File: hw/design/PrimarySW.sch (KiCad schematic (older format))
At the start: 33 parts

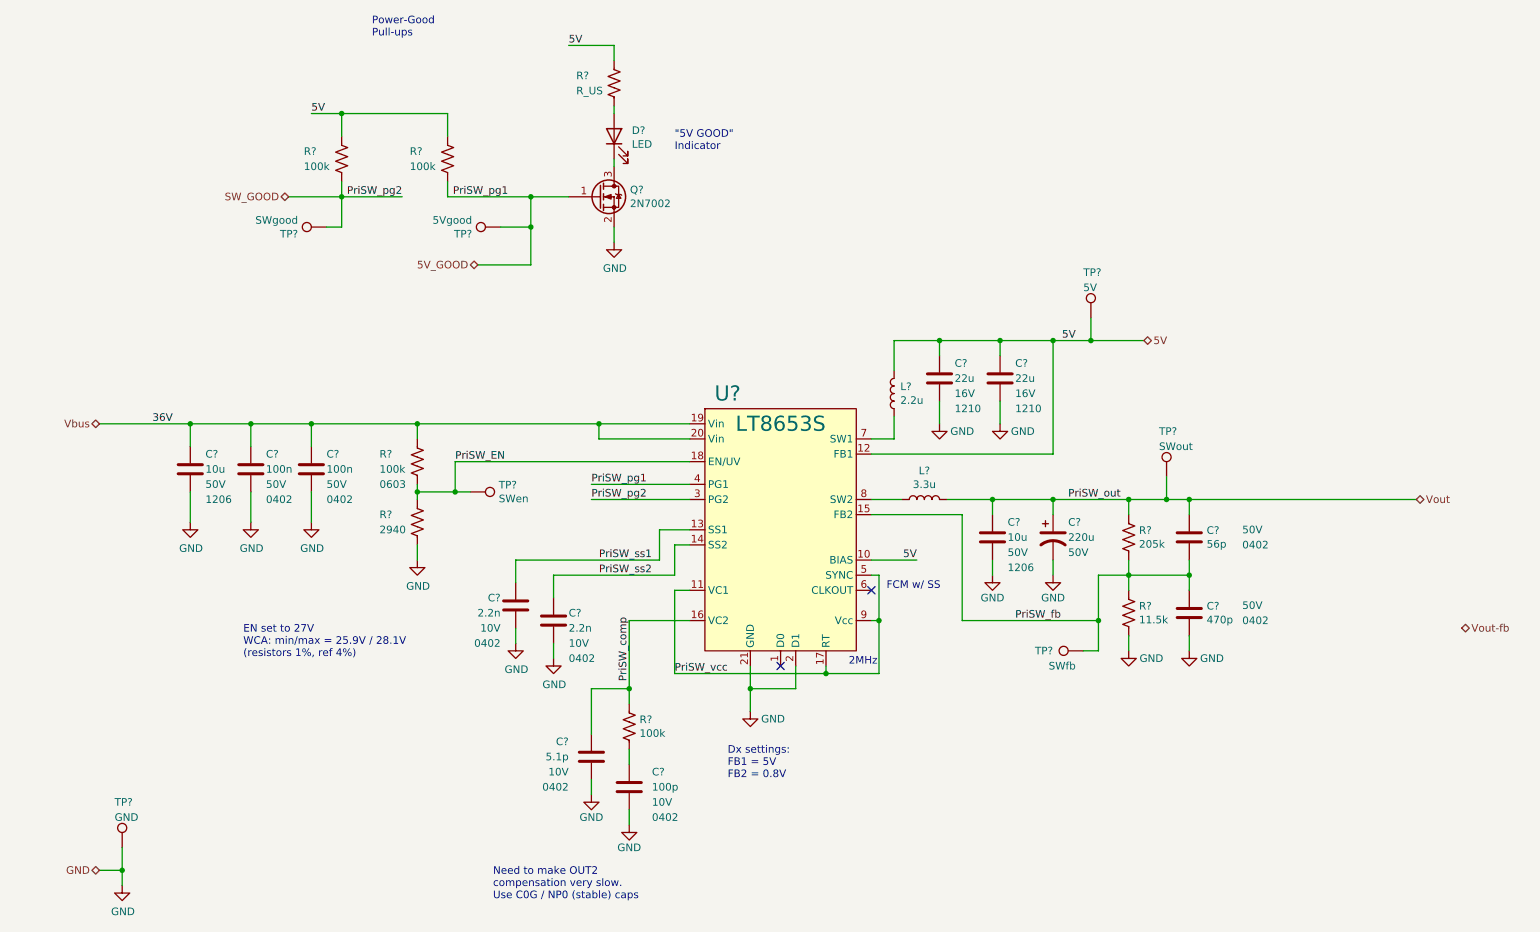
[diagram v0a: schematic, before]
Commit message: label/net reorg, primary SW starting
some reorganization of top-level naming for nets and hierarchical pins

fixed a few part selection issues

started on primary switcher sheet
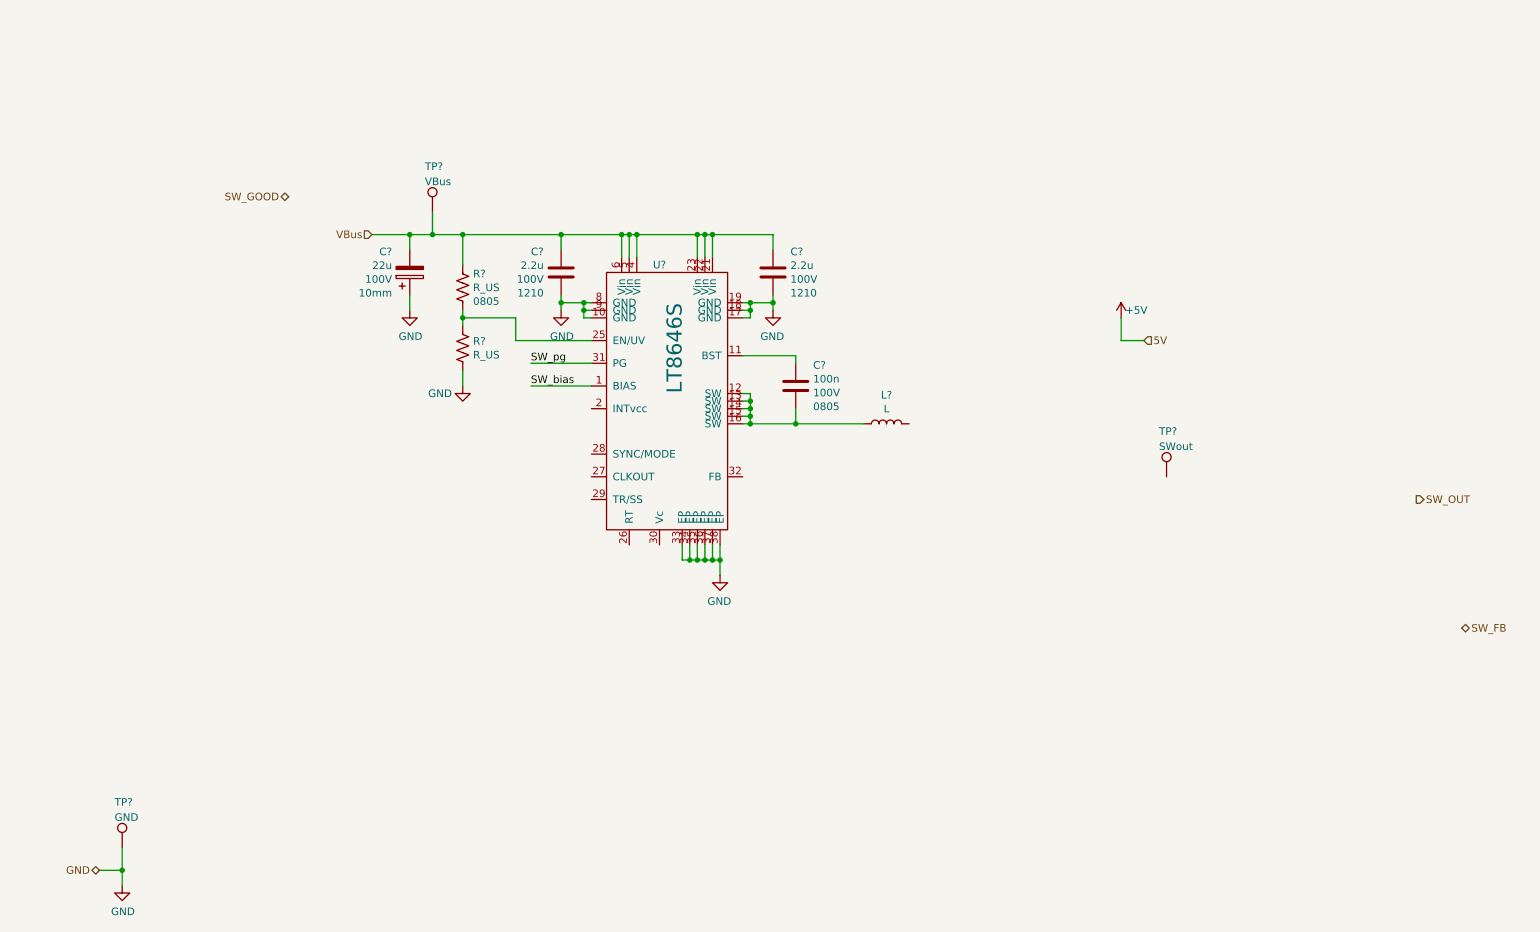
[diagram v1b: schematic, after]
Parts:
- removed C? (x2): 22u, Capacitor_SMD:C_1210_3225Metric_Pad1.42x2.65mm_HandSolder, symbol Device:C
- removed C?: 10u, Resistor_SMD:R_1206_3216Metric_Pad1.42x1.75mm_HandSolder, symbol Device:C
- removed C? (x2): 100n, Capacitor_SMD:C_0603_1608Metric, symbol Device:C
- removed C? (x2): 2.2n, Capacitor_SMD:C_0603_1608Metric, symbol Device:C
- removed C?: 100p, Capacitor_SMD:C_0603_1608Metric, symbol Device:C
- removed C?: 56p, Resistor_SMD:R_0603_1608Metric, symbol Device:C
- removed C?: 470p, Resistor_SMD:R_0603_1608Metric, symbol Device:C
- removed C?: 10u, Capacitor_SMD:C_1206_3216Metric_Pad1.42x1.75mm_HandSolder, symbol Device:C
- removed C?: 220u, symbol Device:CP1
- removed C?: 5.1p, Capacitor_SMD:C_0603_1608Metric, symbol Device:C
- removed D?: LED, LED_SMD:LED_0603_1608Metric, symbol Device:LED
- removed L?: 2.2u, Inductor_SMD:L_Coilcraft_XxL4020, symbol Device:L
- removed L?: 3.3u, Inductor_SMD:L_Coilcraft_XAL5030, symbol Device:L
- removed Q?: 2N7002, Package_TO_SOT_SMD:SOT-323_SC-70, symbol Device:Q_NMOS_GSD
- removed R?: 205k, Resistor_SMD:R_0603_1608Metric, symbol Device:R_US
- removed R?: 11.5k, Resistor_SMD:R_0603_1608Metric, symbol Device:R_US
- removed R? (x3): 100k, Resistor_SMD:R_0603_1608Metric, symbol Device:R_US
- removed R?: 2940, Resistor_SMD:R_0603_1608Metric, symbol Device:R_US
- removed R?: 100k, Resistor_SMD:R_0805_2012Metric, symbol Device:R_US
- removed R?: R_US, Resistor_SMD:R_0603_1608Metric, symbol Device:R_US
- removed TP?: 5V, TestPoint:TestPoint_Keystone_5000-5004_Miniature, symbol Connector:TestPoint
- removed TP?: SWfb, TestPoint:TestPoint_Keystone_5000-5004_Miniature, symbol Connector:TestPoint
- removed TP?: SWgood, TestPoint:TestPoint_Keystone_5000-5004_Miniature, symbol Connector:TestPoint
- removed TP?: 5Vgood, TestPoint:TestPoint_Keystone_5000-5004_Miniature, symbol Connector:TestPoint
- removed TP?: SWen, TestPoint:TestPoint_Keystone_5000-5004_Miniature, symbol Connector:TestPoint
- removed U?: LT8653S, symbol pps_klib:LT8653S
- added C?: 22u, symbol Device:CP
- added C? (x2): 2.2u, Capacitor_SMD:C_1210_3225Metric_Pad1.42x2.65mm_HandSolder, symbol Device:C
- added C?: 100n, symbol Device:C
- added L?: L, symbol Device:L
- added R?: R_US, Resistor_SMD:R_0805_2012Metric_Pad1.15x1.40mm_HandSolder, symbol Device:R_US
- added R?: R_US, Resistor_SMD:R_0603_1608Metric, symbol Device:R_US
- added TP?: VBus, TestPoint:TestPoint_Keystone_5000-5004_Miniature, symbol Connector:TestPoint
- added U?: LT8646S, symbol pps_klib:LT8646S
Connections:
- net GND: now also C?.1, C?.1, C?.1, R?.2, U?.10 (GND), U?.17 (GND), U?.18 (GND), U?.19 (GND), U?.33 (EP), U?.34 (EP), U?.35 (EP), U?.36 (EP), U?.37 (EP), U?.38 (EP), U?.8 (GND), U?.9 (GND)
- net Vout: no longer names the net of TP?.1
- new net: C?.1, U?.11 (BST)
- new net: C?.2, L?.1, U?.12 (SW), U?.13 (SW), U?.14 (SW), U?.15 (SW), U?.16 (SW)
- new net: R?.1, R?.2, U?.25 (EN/UV)
- new net SW_bias: U?.1 (BIAS)
- new net SW_pg: U?.31 (PG)
- new net VBus: C?.2, C?.2, C?.2, R?.1, TP?.1, U?.21 (Vin), U?.22 (Vin), U?.23 (Vin), U?.4 (Vin), U?.5 (Vin), U?.6 (Vin)
- no-connect marks 2 -> 0
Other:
- note removed: ""5V GOOD"\nIndicator"
- note removed: "2MHz"
- note removed: "Dx settings:\nFB1 = 5V\nFB2 = 0.8V"
- note removed: "EN set to 27V\nWCA: min/max = 25.9V / 28.1V\n(resistors 1%, ref 4%)"
- note removed: "FCM w/ SS"
- note removed: "Need to make OUT2\ncompensation very slow.\nUse C0G / NP0 (stable) caps"
- note removed: "Power-Good\nPull-ups"

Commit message: sims, new devices, code started
made some simulations & calculations, started working on code (moved devices into individual header files), new devices chosen in library
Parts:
- removed C?: 22u, symbol Device:CP
- removed C? (x2): 2.2u, Capacitor_SMD:C_1210_3225Metric_Pad1.42x2.65mm_HandSolder, symbol Device:C
- removed C?: 100n, symbol Device:C
- removed L?: L, symbol Device:L
- removed R?: R_US, Resistor_SMD:R_0805_2012Metric_Pad1.15x1.40mm_HandSolder, symbol Device:R_US
- removed R?: R_US, Resistor_SMD:R_0603_1608Metric, symbol Device:R_US
- removed TP?: SWout, TestPoint:TestPoint_Keystone_5000-5004_Miniature, symbol Connector:TestPoint
- removed U?: LT8646S, symbol pps_klib:LT8646S
- added 49.9k, 49.9k?: R_US, Resistor_SMD:R_0603_1608Metric, symbol Device:R_US
- added C? (x3): 1u, Capacitor_SMD:C_0805_2012Metric_Pad1.15x1.40mm_HandSolder, symbol Device:C
- added C?: 1u, Capacitor_SMD:C_0603_1608Metric, symbol Device:C
- added C? (x2): 10n, Capacitor_SMD:C_0603_1608Metric, symbol Device:C
- added C?: 100n, Capacitor_SMD:C_0603_1608Metric, symbol Device:C
- added C? (x5): 10u, Capacitor_SMD:C_1206_3216Metric_Pad1.42x1.75mm_HandSolder, symbol Device:C
- added C?: 220u, symbol Device:CP
- added L?: L, symbol Device:L
- added Q?: 2N3906, Package_TO_SOT_THT:TO-92_Inline, symbol Transistor_BJT:2N3906
- added R? (x2): R_US, symbol Device:R_US
- added R?: 0, Resistor_SMD:R_0603_1608Metric, symbol Device:R_US
- added R?: 1k, symbol Device:R_US
- added U?: LT8637, symbol pps_klib:LT8637
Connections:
- net +5V: now also C?.2, U?.2 (BIAS)
- net GND: now also C?.1, C?.1, C?.1, C?.1, C?.1, C?.1, C?.1, C?.1, C?.1, C?.2, C?.2, R?.1, R?.1, R?.2, U?.13 (GND), U?.21 (EP), U?.4 (GND)
- net SW_FB: now also 49.9k?.1
- net SW_OUT: now also 49.9k.1, C?.1, C?.2, C?.2, C?.2, C?.2, C?.2, L?.2, R?.2
- net VBus: now also C?.1, C?.2, C?.2, U?.11 (VIN), U?.6 (VIN)
- new net: R?.2, U?.15 (SYNC/MODE)
- new net: R?.2, U?.17 (RT)
- new net: C?.2, U?.18 (TR/SS)
- new net: C?.1, Q?.3 (C), R?.1, U?.20 (FB)
- new net: Q?.1 (E), R?.1
- new net: 49.9k.2, 49.9k?.2, Q?.2 (B)
- new net Pre_BST: C?.2, U?.7 (BST)
- new net Pre_EN: U?.14 (EN)
- new net Pre_IVC: C?.2, U?.~ (INTVcc)
- new net Pre_PG: U?.1 (PG)
- new net Pre_SW: C?.1, L?.1, U?.10 (SW), U?.8 (SW), U?.9 (SW)
- no-connect marks 0 -> 1
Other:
- note added: "Ride-On-Top\nFeedback\nCircuit"
- note added: "TR/SS capacitance:\n1.2nF / msec startup"
- moved on the sheet: TP?

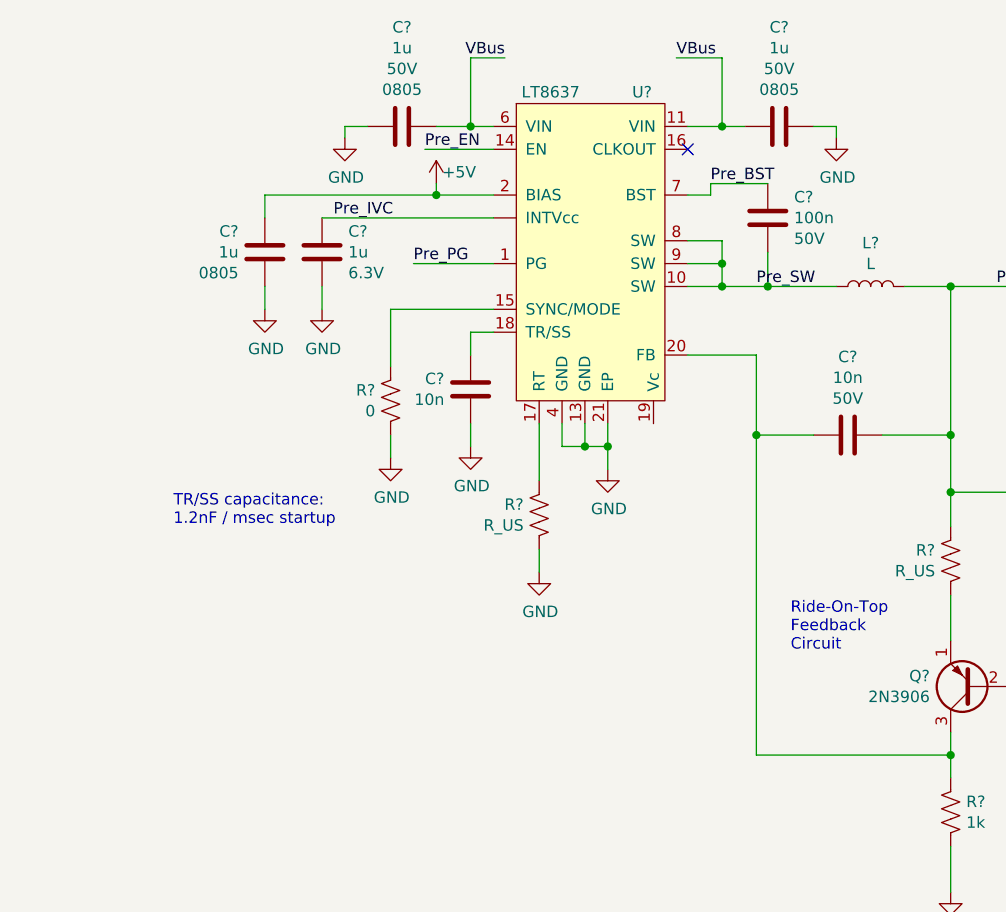
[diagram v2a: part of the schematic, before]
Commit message: rearchitect
new primary switcher : LT8637
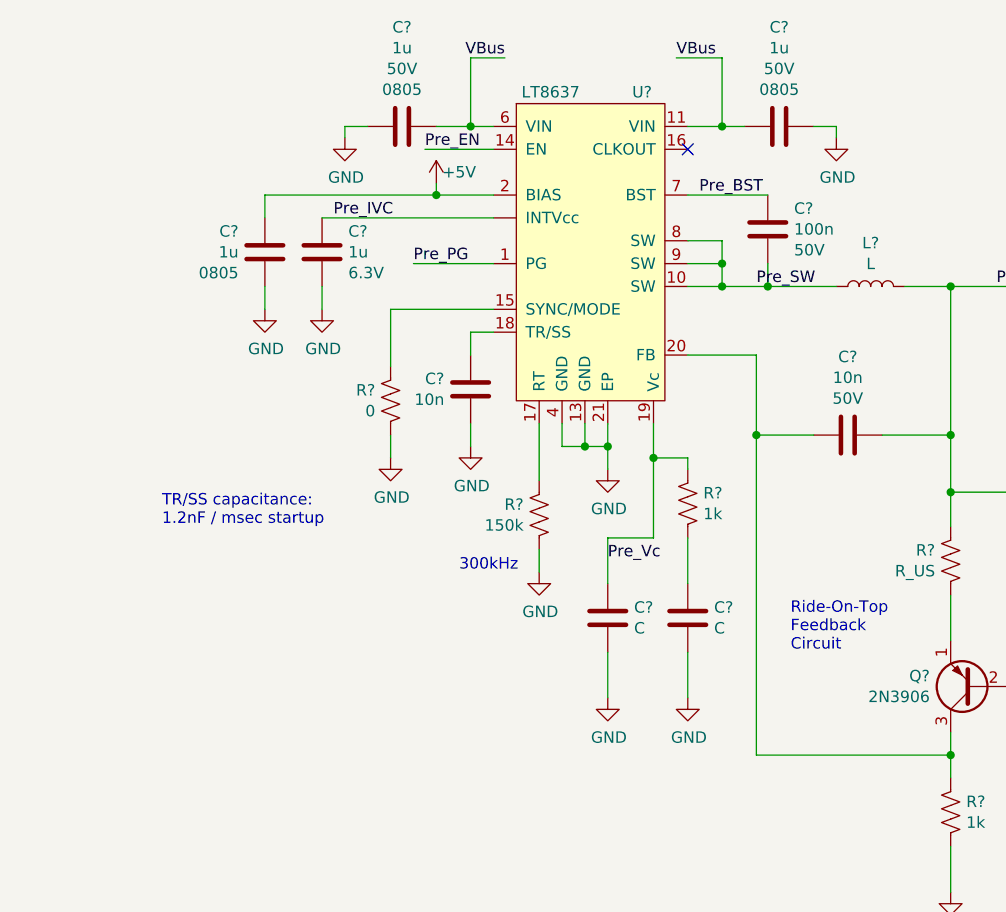
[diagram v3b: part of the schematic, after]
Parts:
- added C? (x2): C, Capacitor_SMD:C_0603_1608Metric, symbol Device:C
- added R?: 1k, Resistor_SMD:R_0603_1608Metric, symbol Device:R_US
- R?: value R_US -> 150k
- R?: footprint (none) -> Resistor_SMD:R_0603_1608Metric
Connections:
- net GND: now also C?.2, C?.2
- net Pre_Vc: now reaches U?.19 (Vc)
- net Pre_Vc: now also C?.1, R?.1
- new net: C?.1, R?.2
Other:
- note added: "300kHz"
- moved on the sheet: C?
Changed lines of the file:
@@
 	1    0    0    1
 $EndComp
-Text Notes 3750 4450 0    50   ~ 0
+Text Notes 3700 4450 0    50   ~ 0
 TR/SS capacitance:\n1.2nF / msec startup
 Wire Wire Line
@@
 L Device:C C?
 U 1 1 606F2507
-P 6350 3100
-F 0 "C?" H 6235 3009 50  0000 R CNN
-F 1 "100n" H 6235 3100 50  0000 R CNN
-F 2 "Capacitor_SMD:C_0603_1608Metric" H 6388 2950 50  0001 C CNN
-F 3 "~" H 6350 3100 50  0001 C CNN
-F 4 "TDK_CGA2B2X5R1C104K050BA" H 6350 3100 50  0001 C CNN "MfrNum"
-F 5 "50V" H 6235 3191 50  0000 R CNN "VRating"
-F 6 "0402" H 6235 3236 50  0001 R CNN "Size"
-	1    6350 3100
+P 6350 3150
+F 0 "C?" H 6235 3059 50  0000 R CNN
+F 1 "100n" H 6235 3150 50  0000 R CNN
+F 2 "Capacitor_SMD:C_0603_1608Metric" H 6388 3000 50  0001 C CNN
+F 3 "~" H 6350 3150 50  0001 C CNN
+F 4 "TDK_CGA2B2X5R1C104K050BA" H 6350 3150 50  0001 C CNN "MfrNum"
+F 5 "50V" H 6235 3241 50  0000 R CNN "VRating"
+F 6 "0402" H 6235 3286 50  0001 R CNN "Size"
+	1    6350 3150
 	-1   0    0    1
 $EndComp
@@
 	6150 3300 6150 3400
 Wire Wire Line
-	6350 3250 6350 3400
+	6350 3300 6350 3400
 Connection ~ 6350 3400
 Wire Wire Line
 	6350 3400 6650 3400
-Wire Wire Line
-	6100 2950 6100 3000
-Wire Wire Line
-	6100 3000 6000 3000
-Wire Wire Line
-	6100 2950 6350 2950
-Text Label 6100 2950 0    50   ~ 0
+Text Label 6050 3000 0    50   ~ 0
 Pre_BST
 Text Label 6300 3400 0    50   ~ 0
@@
 P 5350 4400
 F 0 "R?" H 5282 4354 50  0000 R CNN
-F 1 "R_US" H 5282 4445 50  0000 R CNN
+F 1 "150k" H 5282 4445 50  0000 R CNN
 F 2 "" V 5390 4390 50  0001 C CNN
 F 3 "~" H 5350 4400 50  0001 C CNN
@@
 F 0 "R?" H 7082 5746 50  0000 R CNN
 F 1 "1k" H 7082 5655 50  0000 R CNN
-F 2 "" V 7190 5690 50  0001 C CNN
+F 2 "Resistor_SMD:R_0603_1608Metric" V 7190 5690 50  0001 C CNN
 F 3 "~" H 7150 5700 50  0001 C CNN
 	1    7150 5700
@@
 Text HLabel 1600 1450 0    50   BiDi ~ 0
 SW_GOOD
+Wire Wire Line
+	6000 3000 6350 3000
+Text Notes 5000 4650 0    50   ~ 0
+300kHz
+$Comp
+L Device:R_US R?
+U 1 1 60A996A2
+P 6000 4350
+F 0 "R?" H 5932 4396 50  0000 R CNN
+F 1 "1k" H 5932 4305 50  0000 R CNN
+F 2 "Resistor_SMD:R_0603_1608Metric" V 6040 4340 50  0001 C CNN
+F 3 "~" H 6000 4350 50  0001 C CNN
+	1    6000 4350
+	-1   0    0    -1
+$EndComp
+$Comp
+L Device:C C?
+U 1 1 60A9A1A3
+P 6000 4850
+F 0 "C?" H 6115 4896 50  0000 L CNN
+F 1 "C" H 6115 4805 50  0000 L CNN
+F 2 "Capacitor_SMD:C_0603_1608Metric" H 6038 4700 50  0001 C CNN
+F 3 "~" H 6000 4850 50  0001 C CNN
+	1    6000 4850
+	1    0    0    -1
+$EndComp
+$Comp
+L Device:C C?
+U 1 1 60A9ACE6
+P 5650 4850
+F 0 "C?" H 5765 4896 50  0000 L CNN
+F 1 "C" H 5765 4805 50  0000 L CNN
+F 2 "Capacitor_SMD:C_0603_1608Metric" H 5688 4700 50  0001 C CNN
+F 3 "~" H 5650 4850 50  0001 C CNN
+	1    5650 4850
+	1    0    0    -1
+$EndComp
+Wire Wire Line
+	5850 4000 5850 4150
+Wire Wire Line
+	5850 4500 5650 4500
+Wire Wire Line
+	5650 4500 5650 4700
+Wire Wire Line
+	6000 4200 6000 4150
+Wire Wire Line
+	6000 4150 5850 4150
+Connection ~ 5850 4150
+Wire Wire Line
+	5850 4150 5850 4500
+Wire Wire Line
+	6000 4500 6000 4700
+$Comp
+L power:GND #PWR?
+U 1 1 60AA1EAD
+P 5650 5200
+AR Path="/60AA1EAD" Ref="#PWR?"  Part="1"
+AR Path="/604399F3/60AA1EAD" Ref="#PWR?"  Part="1"
+AR Path="/602B8B91/60AA1EAD" Ref="#PWR?"  Part="1"
+F 0 "#PWR?" H 5650 4950 50  0001 C CNN
+F 1 "GND" H 5655 5027 50  0000 C CNN
+F 2 "" H 5650 5200 50  0001 C CNN
+F 3 "" H 5650 5200 50  0001 C CNN
+	1    5650 5200
+	1    0    0    -1
+$EndComp
+$Comp
+L power:GND #PWR?
+U 1 1 60AA1FFA
+P 6000 5200
+AR Path="/60AA1FFA" Ref="#PWR?"  Part="1"
+AR Path="/604399F3/60AA1FFA" Ref="#PWR?"  Part="1"
+AR Path="/602B8B91/60AA1FFA" Ref="#PWR?"  Part="1"
+F 0 "#PWR?" H 6000 4950 50  0001 C CNN
+F 1 "GND" H 6005 5027 50  0000 C CNN
+F 2 "" H 6000 5200 50  0001 C CNN
+F 3 "" H 6000 5200 50  0001 C CNN
+	1    6000 5200
+	1    0    0    -1
+$EndComp
+Wire Wire Line
+	6000 5200 6000 5000
+Wire Wire Line
+	5650 5000 5650 5200
+Text Label 5650 4600 0    50   ~ 0
+Pre_Vc
 $EndSCHEMATC
